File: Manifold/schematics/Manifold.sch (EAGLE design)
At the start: 124 parts, among them IC1 MC7805CDTG, IC2 NE5532D, IC3 NE5532D, IC4 QUAD_OPAMPD, IC5 LM4040B10, IC6 TL072D, Q1 BSS123, Q2 SI2309CDS

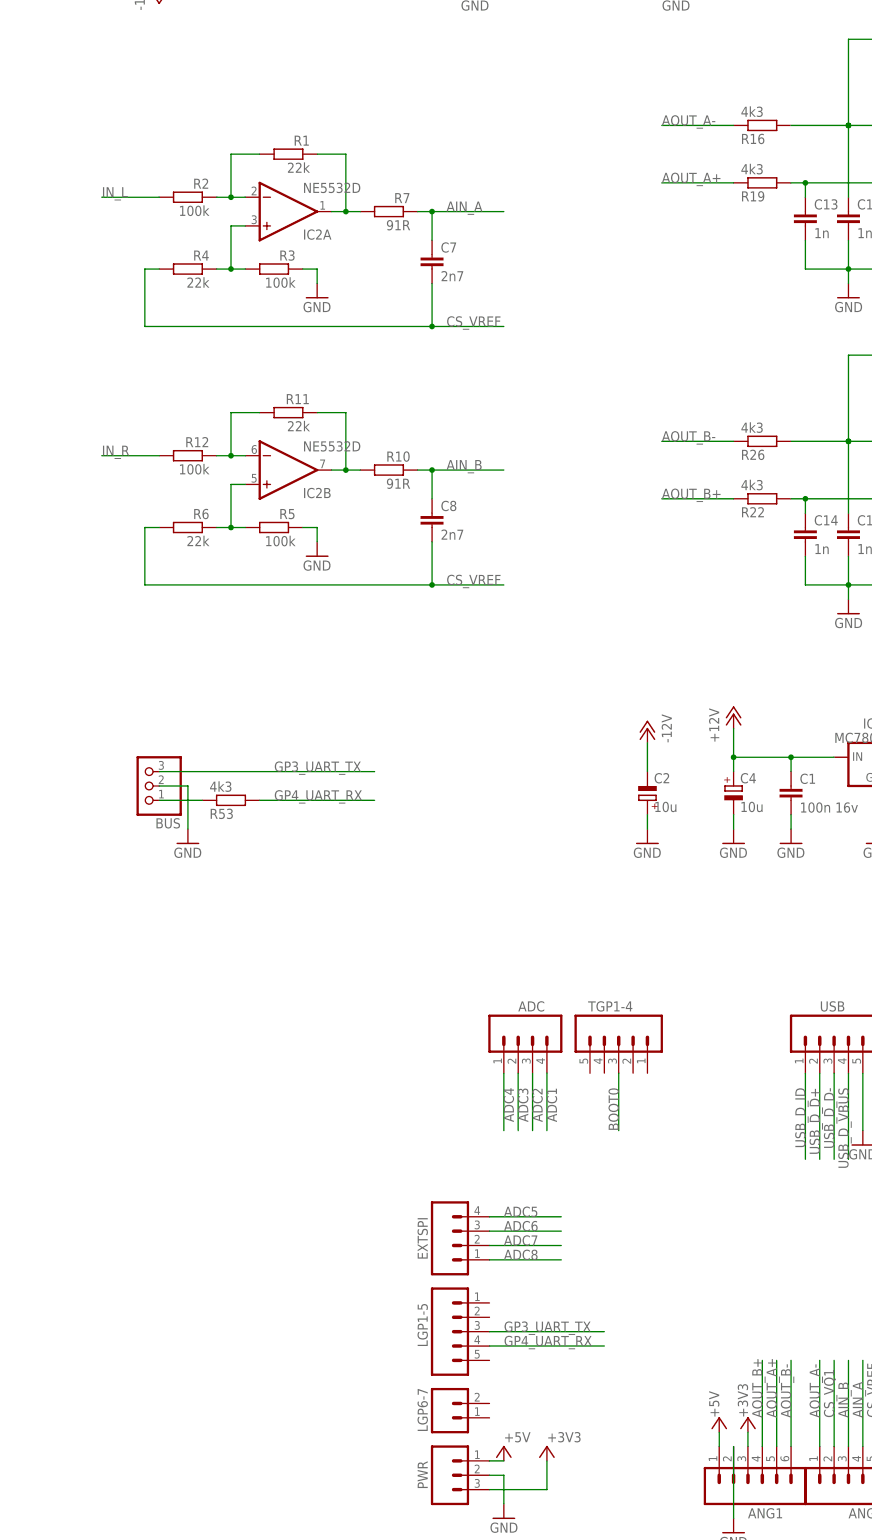
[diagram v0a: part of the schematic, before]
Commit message: change resistor value
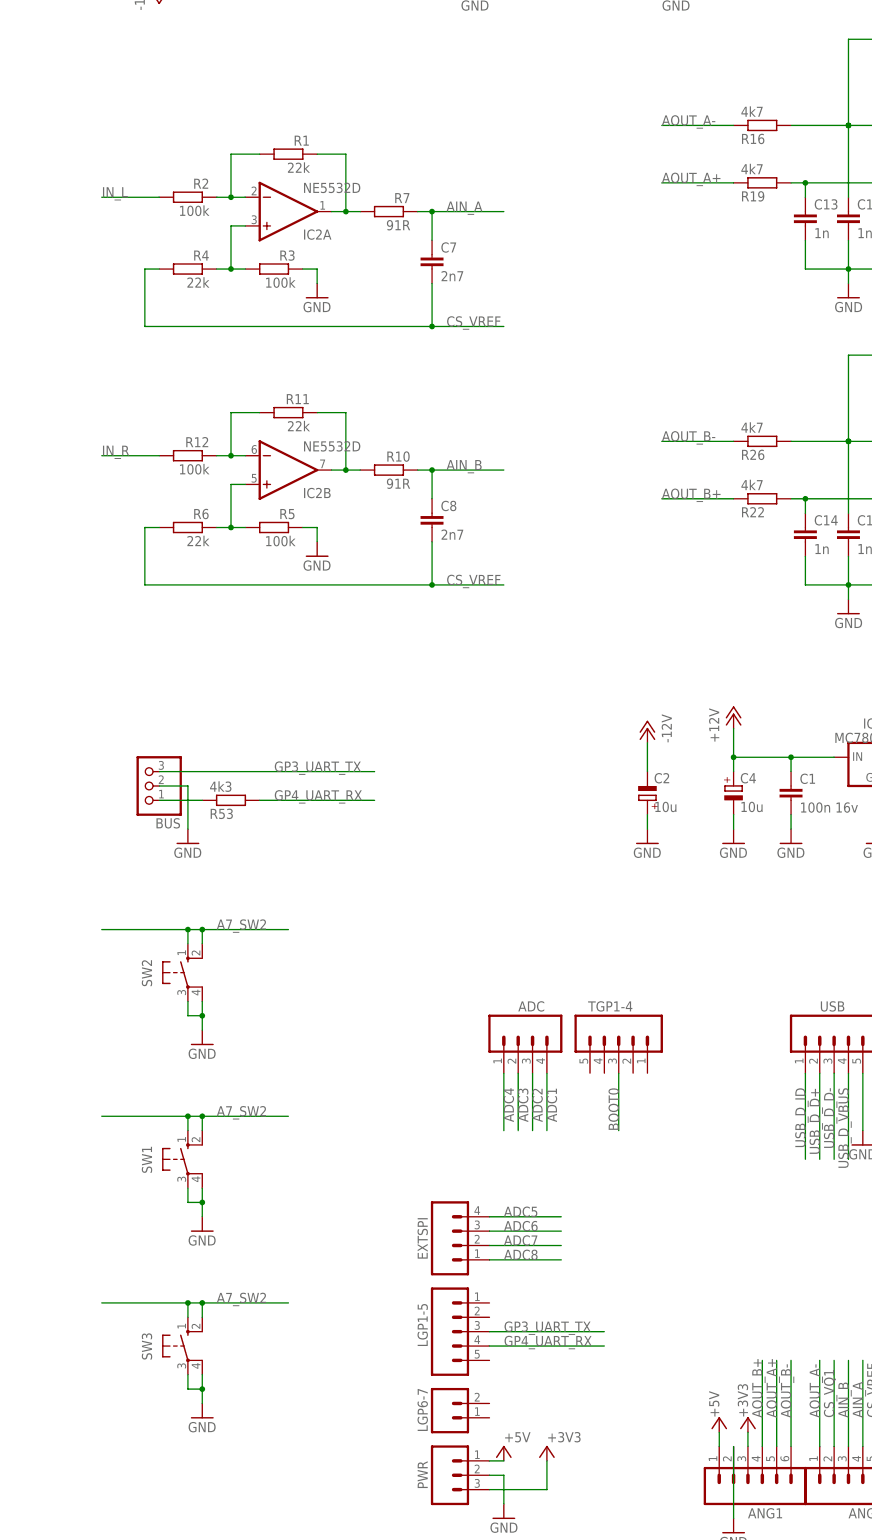
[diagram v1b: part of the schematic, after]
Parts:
- added SW1, SW2, SW3: (no value), switch-omron:10-XX
- R16, R19, R22, R26: value 4k3 -> 4k7
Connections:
- new net A7_SW2: SW1.S, SW1.S1, SW2.S, SW2.S1, SW3.S, SW3.S1
- net GND: now also SW1.P, SW1.P1, SW2.P, SW2.P1, SW3.P, SW3.P1
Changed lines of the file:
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@@
 <layer number="59" name="tCarbon" color="7" fill="1" visible="no" active="no"/>
 <layer number="60" name="bCarbon" color="7" fill="1" visible="no" active="no"/>
+<layer number="88" name="SimResults" color="9" fill="1" visible="no" active="yes"/>
+<layer number="89" name="SimProbes" color="9" fill="1" visible="no" active="yes"/>
 <layer number="90" name="Modules" color="5" fill="1" visible="yes" active="yes"/>
 <layer number="91" name="Nets" color="2" fill="1" visible="yes" active="yes"/>
@@
 <part name="R14" library="Rebel" deviceset="R-EU_" device="0603" value="10k"/>
 <part name="R13" library="Rebel" deviceset="R-EU_" device="0603" value="1k"/>
-<part name="R16" library="Rebel" deviceset="R-EU_" device="0603" value="4k3"/>
+<part name="R16" library="Rebel" deviceset="R-EU_" device="0603" value="4k7"/>
 <part name="PWR" library="SparkFun" deviceset="M03" device="PTH"/>
 <part name="P+8" library="supply1" deviceset="+5V" device=""/>
@@
 <part name="CVY_L" library="Rebel" deviceset="THONKICONN" device=""/>
 <part name="CVY_R" library="Rebel" deviceset="THONKICONN" device=""/>
-<part name="R19" library="Rebel" deviceset="R-EU_" device="0603" value="4k3"/>
+<part name="R19" library="Rebel" deviceset="R-EU_" device="0603" value="4k7"/>
 <part name="GND19" library="supply1" deviceset="GND" device=""/>
 <part name="GND14" library="supply1" deviceset="GND" device=""/>
@@
 <part name="R28" library="Rebel" deviceset="R-EU_" device="0603" value="10k"/>
 <part name="R27" library="Rebel" deviceset="R-EU_" device="0603" value="1k"/>
-<part name="R26" library="Rebel" deviceset="R-EU_" device="0603" value="4k3"/>
-<part name="R22" library="Rebel" deviceset="R-EU_" device="0603" value="4k3"/>
+<part name="R26" library="Rebel" deviceset="R-EU_" device="0603" value="4k7"/>
+<part name="R22" library="Rebel" deviceset="R-EU_" device="0603" value="4k7"/>
 <part name="GND15" library="supply1" deviceset="GND" device=""/>
 <part name="R25" library="Rebel" deviceset="R-EU_" device="0603" value="4k7"/>
@@
 <part name="GND21" library="supply1" deviceset="GND" device=""/>
 <part name="GND40" library="supply1" deviceset="GND" device=""/>
+<part name="SW2" library="switch-omron" deviceset="10-XX" device=""/>
+<part name="GND50" library="supply1" deviceset="GND" device=""/>
+<part name="SW1" library="switch-omron" deviceset="10-XX" device=""/>
+<part name="GND51" library="supply1" deviceset="GND" device=""/>
+<part name="SW3" library="switch-omron" deviceset="10-XX" device=""/>
+<part name="GND53" library="supply1" deviceset="GND" device=""/>
 </parts>
 <sheets>
@@
 <instance part="POTTUNE_L" gate="G$2" x="-22.86" y="256.54" smashed="yes"/>
 <instance part="POTTUNE_R" gate="G$2" x="-12.7" y="256.54" smashed="yes"/>
+<instance part="SW2" gate="1" x="50.8" y="58.42" smashed="yes">
+<attribute name="NAME" x="44.45" y="55.88" size="1.778" layer="95" rot="R90"/>
+<attribute name="VALUE" x="46.99" y="61.595" size="1.778" layer="96" rot="R90"/>
+</instance>
+<instance part="GND50" gate="1" x="53.34" y="45.72" smashed="yes">
+<attribute name="VALUE" x="50.8" y="43.18" size="1.778" layer="96"/>
+</instance>
+<instance part="SW1" gate="1" x="50.8" y="25.4" smashed="yes">
+<attribute name="NAME" x="44.45" y="22.86" size="1.778" layer="95" rot="R90"/>
+<attribute name="VALUE" x="46.99" y="28.575" size="1.778" layer="96" rot="R90"/>
+</instance>
+<instance part="GND51" gate="1" x="53.34" y="12.7" smashed="yes">
+<attribute name="VALUE" x="50.8" y="10.16" size="1.778" layer="96"/>
+</instance>
+<instance part="SW3" gate="1" x="50.8" y="-7.62" smashed="yes">
+<attribute name="NAME" x="44.45" y="-10.16" size="1.778" layer="95" rot="R90"/>
+<attribute name="VALUE" x="46.99" y="-4.445" size="1.778" layer="96" rot="R90"/>
+</instance>
+<instance part="GND53" gate="1" x="53.34" y="-20.32" smashed="yes">
+<attribute name="VALUE" x="50.8" y="-22.86" size="1.778" layer="96"/>
+</instance>
 </instances>
 <busses>
@@
 <wire x1="22.86" y1="238.76" x2="20.32" y2="238.76" width="0.1524" layer="91"/>
 </segment>
+<segment>
+<pinref part="GND50" gate="1" pin="GND"/>
+<pinref part="SW2" gate="1" pin="P1"/>
+<wire x1="53.34" y1="48.26" x2="53.34" y2="50.8" width="0.1524" layer="91"/>
+<pinref part="SW2" gate="1" pin="P"/>
+<wire x1="53.34" y1="50.8" x2="53.34" y2="53.34" width="0.1524" layer="91"/>
+<wire x1="53.34" y1="50.8" x2="50.8" y2="50.8" width="0.1524" layer="91"/>
+<wire x1="50.8" y1="50.8" x2="50.8" y2="53.34" width="0.1524" layer="91"/>
+<junction x="53.34" y="50.8"/>
+</segment>
+<segment>
+<pinref part="GND51" gate="1" pin="GND"/>
+<pinref part="SW1" gate="1" pin="P1"/>
+<wire x1="53.34" y1="15.24" x2="53.34" y2="17.78" width="0.1524" layer="91"/>
+<pinref part="SW1" gate="1" pin="P"/>
+<wire x1="53.34" y1="17.78" x2="53.34" y2="20.32" width="0.1524" layer="91"/>
+<wire x1="53.34" y1="17.78" x2="50.8" y2="17.78" width="0.1524" layer="91"/>
+<wire x1="50.8" y1="17.78" x2="50.8" y2="20.32" width="0.1524" layer="91"/>
+<junction x="53.34" y="17.78"/>
+</segment>
+<segment>
+<pinref part="GND53" gate="1" pin="GND"/>
+<pinref part="SW3" gate="1" pin="P1"/>
+<wire x1="53.34" y1="-17.78" x2="53.34" y2="-15.24" width="0.1524" layer="91"/>
+<pinref part="SW3" gate="1" pin="P"/>
+<wire x1="53.34" y1="-15.24" x2="53.34" y2="-12.7" width="0.1524" layer="91"/>
+<wire x1="53.34" y1="-15.24" x2="50.8" y2="-15.24" width="0.1524" layer="91"/>
+<wire x1="50.8" y1="-15.24" x2="50.8" y2="-12.7" width="0.1524" layer="91"/>
+<junction x="53.34" y="-15.24"/>
+</segment>
 </net>
 <net name="+5V" class="0">
@@
 </segment>
 </net>
+<net name="A7_SW2" class="0">
+<segment>
+<pinref part="SW2" gate="1" pin="S1"/>
+<wire x1="50.8" y1="66.04" x2="53.34" y2="66.04" width="0.1524" layer="91"/>
+<wire x1="53.34" y1="63.5" x2="53.34" y2="66.04" width="0.1524" layer="91"/>
+<pinref part="SW2" gate="1" pin="S"/>
+<wire x1="50.8" y1="63.5" x2="50.8" y2="66.04" width="0.1524" layer="91"/>
+<junction x="50.8" y="66.04"/>
+<wire x1="35.56" y1="66.04" x2="50.8" y2="66.04" width="0.1524" layer="91"/>
+<label x="55.88" y="66.04" size="1.778" layer="95"/>
+<wire x1="53.34" y1="66.04" x2="68.58" y2="66.04" width="0.1524" layer="91"/>
+<junction x="53.34" y="66.04"/>
+</segment>
+<segment>
+<pinref part="SW1" gate="1" pin="S1"/>
+<wire x1="50.8" y1="33.02" x2="53.34" y2="33.02" width="0.1524" layer="91"/>
+<wire x1="53.34" y1="30.48" x2="53.34" y2="33.02" width="0.1524" layer="91"/>
+<pinref part="SW1" gate="1" pin="S"/>
+<wire x1="50.8" y1="30.48" x2="50.8" y2="33.02" width="0.1524" layer="91"/>
+<junction x="50.8" y="33.02"/>
+<wire x1="35.56" y1="33.02" x2="50.8" y2="33.02" width="0.1524" layer="91"/>
+<label x="55.88" y="33.02" size="1.778" layer="95"/>
+<wire x1="53.34" y1="33.02" x2="68.58" y2="33.02" width="0.1524" layer="91"/>
+<junction x="53.34" y="33.02"/>
+</segment>
+<segment>
+<pinref part="SW3" gate="1" pin="S1"/>
+<wire x1="50.8" y1="0" x2="53.34" y2="0" width="0.1524" layer="91"/>
+<wire x1="53.34" y1="-2.54" x2="53.34" y2="0" width="0.1524" layer="91"/>
+<pinref part="SW3" gate="1" pin="S"/>
+<wire x1="50.8" y1="-2.54" x2="50.8" y2="0" width="0.1524" layer="91"/>
+<junction x="50.8" y="0"/>
+<wire x1="35.56" y1="0" x2="50.8" y2="0" width="0.1524" layer="91"/>
+<label x="55.88" y="0" size="1.778" layer="95"/>
+<wire x1="53.34" y1="0" x2="68.58" y2="0" width="0.1524" layer="91"/>
+<junction x="53.34" y="0"/>
+</segment>
+</net>
